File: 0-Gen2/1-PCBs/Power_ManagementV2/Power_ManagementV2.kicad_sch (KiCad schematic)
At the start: 81 parts, among them J10 Conn_01x02_Pin, J11 SBH11-PBPC-D10-ST-BK, J3 Conn_01x08, J4 Conn_01x08, J7 Conn_01x02_Pin, J8 Conn_01x02_Pin, J9 Conn_01x02_Pin, Q10 MCTL160N15Y-TP, Q11 MCTL160N15Y-TP, Q12 MCTL160N15Y-TP, Q7 MCTL160N15Y-TP, Q8 MCTL160N15Y-TP, Q9 MCTL160N15Y-TP, U15 STPS5045SG-TR, U16 STPS5045SG-TR, U17 BA033CC0FP-E2, U18 LTC1255CS8-PBF, U7 ACS758LCB-100U-PFF-T

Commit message: almost done with layout
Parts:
- removed JP18: Jumper_2_Open, Jumper:SolderJumper-2_P1.3mm_Open_RoundedPad1.0x1.5mm, symbol Jumper:Jumper_2_Open
- added H2: MountingHole, MountingHole:MountingHole_3.2mm_M3, symbol Mechanical:MountingHole
- added J7: USB_A_Stacked, Connector_USB:USB_A_Wuerth_61400826021_Horizontal_Stacked, symbol Connector:USB_A_Stacked
- added JP12: Jumper_2_Open, Imported_Footprints:KEYSTONE_5102, symbol Jumper:Jumper_2_Open
- added JP18: Jumper_2_Bridged, Jumper:SolderJumper-2_P1.3mm_Bridged2Bar_RoundedPad1.0x1.5mm, symbol Jumper:Jumper_2_Bridged
- added R16: 10k, Resistor_SMD:R_0805_2012Metric_Pad1.20x1.40mm_HandSolder, symbol Device:R_US
- added U14: MCP9808_MSOP, Package_SO:MSOP-8_3x3mm_P0.65mm, symbol Sensor_Temperature:MCP9808_MSOP
- J1: renamed from J8; footprint Connector_AMASS:AMASS_XT60-F_1x02_P7.20mm_Vertical -> Connector_AMASS:AMASS_XT60-M_1x02_P7.20mm_Vertical
- J2: renamed from J7; footprint Connector_AMASS:AMASS_XT60-F_1x02_P7.20mm_Vertical -> Connector_AMASS:AMASS_XT60-M_1x02_P7.20mm_Vertical
- J5: renamed from J9; footprint Connector_AMASS:AMASS_XT60-M_1x02_P7.20mm_Vertical -> Connector_AMASS:AMASS_XT60PW-F_1x02_P7.20mm_Horizontal
- J6: renamed from J10; footprint Connector_AMASS:AMASS_XT60-M_1x02_P7.20mm_Vertical -> Connector_AMASS:AMASS_XT30PW-F_1x02_P2.50mm_Horizontal
- J8: renamed from J11; footprint ImportedV2:SULLINS_SBH11-PBPC-D10-ST-BK -> Imported_Footprints:SULLINS_SBH11-PBPC-D10-ST-BK
- renumbered C19 to C1, C21 to C10, C22 to C11, C14 to C2, C15 to C3, C16 to C4, C17 to C5, C18 to C6, C3 to C7, C4 to C8, C20 to C9, CR2 to CR1, D11 to D1, D12 to D2, D13 to D3, H2 to H5, JP15 to JP1, JP5 to JP10, JP7 to JP11, JP35 to JP13, JP32 to JP14, JP34 to JP15, JP31 to JP16, JP33 to JP17, JP36 to JP19, JP16 to JP2, JP37 to JP20, JP17 to JP3, JP28 to JP4, JP27 to JP5, JP29 to JP6, JP26 to JP7, JP30 to JP8, JP4 to JP9, PM3 to PM1, PM4 to PM2, Q7 to Q1, Q8 to Q2, Q9 to Q3, Q10 to Q4, Q11 to Q5, Q12 to Q6, R22 to R1, R38 to R10, R41 to R11, R39 to R12, R27 to R13, R29 to R14, R28 to R15, R23 to R2, R24 to R3, R25 to R4, R26 to R5, R20 to R6, R19 to R7, R21 to R8, R40 to R9, TH3 to TH1, TH4 to TH2, TP2 to TP1, TP7 to TP2, TP6 to TP3, TP5 to TP4, TP3 to TP5, TP4 to TP6, U15 to U1, U16 to U2, U18 to U3, U17 to U4, U7 to U5
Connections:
- net +3.3V: now also R16.1, U14.5 (A2), U14.6 (A1), U14.7 (A0), U14.8 (V_{DD})
- net +BATT: now also JP12.2 (B)
- net -BATT1: now also J7.4 (GND1), J7.8 (GND2), JP18.1 (A), R16.2, U14.4 (GND)
- net Device_D+: now also J7.3 (D1+), J7.7 (D2+)
- net Device_D-: now also J7.2 (D1-), J7.6 (D2-)
- net I2C1_SCL: now also U14.2 (SCL)
- net I2C1_SDA: now also U14.1 (SDA)
- net at C10.1, C11.1, R14.2: now also JP12.1 (A)
- new net: J7.9 (Shield), JP18.2 (B)
- no-connect marks 3 -> 7
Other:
- added sheet Neopixels (NEOs.kicad_sch)
- note added: "I2C @ 0x1F format: 0011(A2)(A1)(A0)"
- note added: "Integrated MCP9808 #1"
- note added: "USB Passthrough (Teensy Orin/Teensy Dev Port)"
- moved on the sheet: H1, H3, H4

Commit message: done with dist
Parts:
- added J9: Conn_01x04_Pin, Imported_Footprints:CONN_SD-43045-008_04_MOL, symbol Connector:Conn_01x04_Pin
- added JP28: Jumper_3_Bridged12, Jumper:SolderJumper-3_P1.3mm_Bridged2Bar12_RoundedPad1.0x1.5mm, symbol Jumper:Jumper_3_Bridged12
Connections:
- net +3.3V: now also JP28.3 (B)
- net +5V: now also JP28.1 (A)
- net -BATT1: now also J9.2 (Pin_2)
- net I2C1_SCL: now also J9.4 (Pin_4)
- net I2C1_SDA: now also J9.3 (Pin_3)
- new net: J9.1 (Pin_1), JP28.2 (C)
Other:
- note added: "Screen I2C"
- moved on the sheet: R16, U14

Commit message: almost done with all orders
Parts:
- J1, J2: footprint Connector_AMASS:AMASS_XT60-M_1x02_P7.20mm_Vertical -> Connector_AMASS:AMASS_XT60IPW-M_1x03_P7.20mm_Horizontal
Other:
- note removed: "Todo: verify xt60 orientation"
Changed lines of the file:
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@@
 		)
 	)
-	(text "Todo:\nverify xt60 orientation"
-		(exclude_from_sim no)
-		(at -55.753 57.15 0)
-		(effects
-			(font
-				(size 1.27 1.27)
-			)
-			(justify left)
-		)
-	)
 	(text "https://learn.adafruit.com/adafruit-ads7830-8-channel-8-bit-adc/pinouts"
 		(exclude_from_sim no)
@@
 			)
 		)
-		(property "Footprint" "Connector_AMASS:AMASS_XT60-M_1x02_P7.20mm_Vertical"
+		(property "Footprint" "Connector_AMASS:AMASS_XT60IPW-M_1x03_P7.20mm_Horizontal"
 			(at 24.257 59.563 0)
 			(effects
@@
 			)
 		)
-		(property "Footprint" "Connector_AMASS:AMASS_XT60-M_1x02_P7.20mm_Vertical"
+		(property "Footprint" "Connector_AMASS:AMASS_XT60IPW-M_1x03_P7.20mm_Horizontal"
 			(at 24.384 41.783 0)
 			(effects

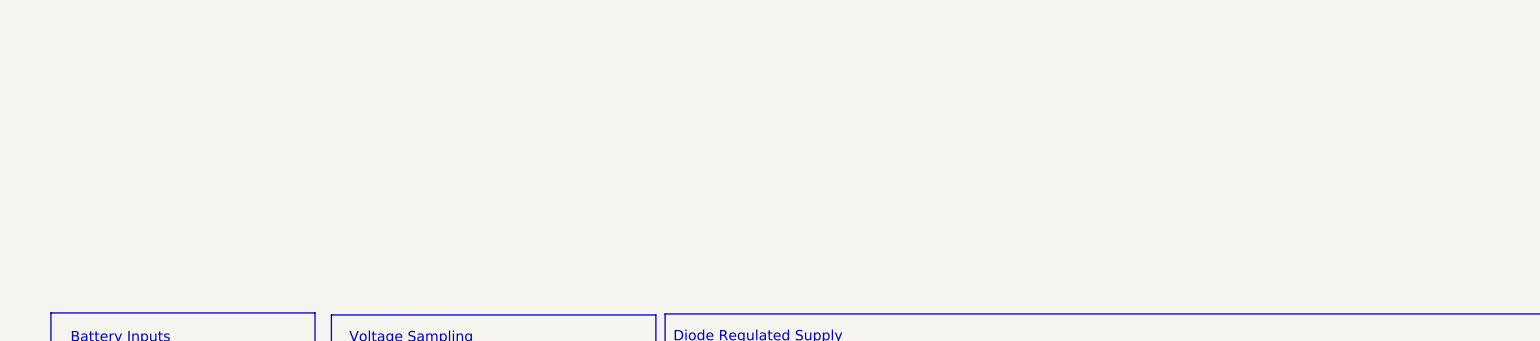
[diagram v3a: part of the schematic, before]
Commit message: [bugfixing] board bringup
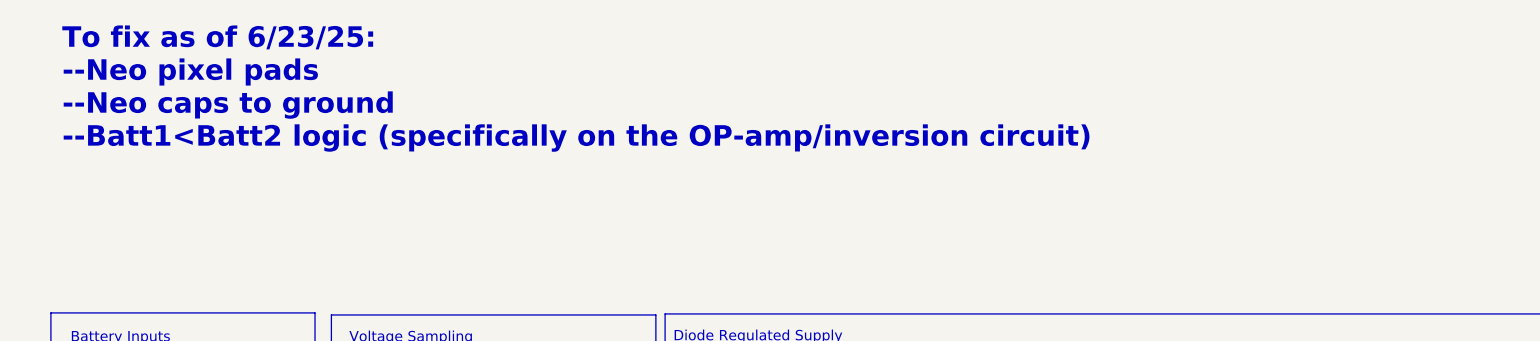
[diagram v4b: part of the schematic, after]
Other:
- note added: "To fix as of 6/23/25: --Neo pixel pads --Neo caps to ground --Batt1<Batt2 logic (specifically on the OP-amp/inversion circuit)"
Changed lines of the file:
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@@
 		)
 	)
+	(text "To fix as of 6/23/25:\n--Neo pixel pads\n--Neo caps to ground\n--Batt1<Batt2 logic (specifically on the OP-amp/inversion circuit)\n"
+		(exclude_from_sim no)
+		(at 17.145 -3.048 0)
+		(effects
+			(font
+				(size 2.54 2.54)
+				(thickness 0.508)
+				(bold yes)
+				(color 132 0 0 1)
+			)
+			(justify left)
+		)
+	)
 	(text "Make sure to put IP+ and IP- contacts\nas close to the power trace as possible"
 		(exclude_from_sim no)
@@
 			(effects
 				(font
+					(size 1.27 1.27)
+				)
+				(hide yes)
+			)
+		)
+		(property "MFR" ""
+			(at 136.779 39.624 0)
+			(effects
+				(font
+					(size 1.27 1.27)
+				)
+				(hide yes)
+			)
+		)
+		(property "MFR S/N" ""
+			(at 136.779 39.624 0)
+			(effects
+				(font
+					(size 1.27 1.27)
+				)
+				(hide yes)
+			)
+		)
+		(property "Supplier 2" ""
+			(at 136.779 39.624 0)
+			(effects
+				(font
+					(size 1.27 1.27)
+				)
+				(hide yes)
+			)
+		)
+		(property "Supplier 2 S/N" ""
+			(at 136.779 39.624 0)
+			(effects
+				(font
